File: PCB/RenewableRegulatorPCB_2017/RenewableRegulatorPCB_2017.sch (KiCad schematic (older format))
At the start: 39 parts, among them IC1 ATTINY84-P, K1 IO_0-2, K2 PWR, P1 INPUT, P2 ISP, P3 FTDI_OUTPUT, P4 DUMP1, P5 DUMP2, Q1 MOSFET_N, Q2 MOSFET_N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

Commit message: Updated PCB
First version of schematic. Needs review
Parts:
- removed C1: 10uf, symbol CP1-RESCUE-RenewableRegulatorPCB_2017
- removed C2: 100u, symbol CP1-RESCUE-RenewableRegulatorPCB_2017
- removed C4, C5: 100n, symbol C-RESCUE-RenewableRegulatorPCB_2017
- removed D1: 1N4001, symbol DIODE
- removed D3: RGB_LED, ~, symbol RGB_LED
- removed D4, D6: LED, symbol LED-RESCUE-RenewableRegulatorPCB_2017
- removed D5, D7: UF4001, symbol DIODE
- removed IC1: ATTINY84-P, DIP14, symbol ATTINY84-P-RESCUE-RenewableRegulatorPCB_2017
- removed K1: IO_0-2, symbol CONN_3
- removed K2: PWR, symbol CONN_3
- removed MH4: CONN_1, symbol CONN_1
- removed P2: ISP, symbol CONN_3X2
- removed P3: FTDI_OUTPUT, symbol CONN_6
- removed P4: DUMP1, symbol CONN_2
- removed Q1, Q2: MOSFET_N, symbol MOSFET_N
- removed R5: R, symbol R-RESCUE-RenewableRegulatorPCB_2017
- removed R6, R8: 1k, symbol R-RESCUE-RenewableRegulatorPCB_2017
- removed R7, R9: 100k, symbol R-RESCUE-RenewableRegulatorPCB_2017
- removed RV1, RV2: POT, symbol POT-RESCUE-RenewableRegulatorPCB_2017
- removed U1: 7805/LM2931, symbol 7805
- removed U2: TC427, ~, symbol TC427
- added C2: 100nf, matts_components:C1_wide_lg_pad, symbol C-RESCUE-RenewableRegulatorPCB_2017
- added C3: 100uf, REInnovationFootprint:C_1V7_TH, symbol CP
- added D2: 3v3, REInnovationFootprint:TH_Diode_1, symbol ZENER-RESCUE-RenewableRegulatorPCB_2017
- added D3, D4: 1N5819, REInnovationFootprint:TH_Diode_1, symbol D
- added D5: WS2811_5mm, REInnovationFootprint:TH_WS2811_LED_8mm, symbol WS2811_5mm
- added DISP1: OLED_I2C, matts_components:SIL-4_large_pad, symbol OLED_I2C
- added DISP2: SPI_LCD, matts_components:SIL-8_lg_pad_1mm, symbol CONN_01X08
- added ENC1: Encoder, REInnovationFootprint:TH_Encoder, symbol Encoder_1
- added F1: 1A, REInnovationFootprint:TH_MC36188_FUSE, symbol FUSE
- added J1: Arduino_Nano_Header, REInnovationFootprint:NANO_DIP_30_600, symbol Arduino_Nano_Header
- added J?: JACK_TRS_6PINS, symbol JACK_TRS_6PINS
- added P2: Vref?, matts_components:SIL-2_solder_connect, symbol CONN_01X02
- added P3: MicroSD, matts_components:SIL-6_large_pads_marker, symbol CONN_01X06
- added P4: SERIAL, matts_components:SIL-4_Grove_SIL, symbol CONN_01X04
- added VR1, VR2: VR, REInnovationFootprint:TH_MC36188_FUSE, symbol VR
- C1: renamed from C3; value 100n -> 100nf; footprint (none) -> matts_components:C1_wide_lg_pad
- D1: renamed from D2; value 5v1 -> 3v3; footprint (none) -> REInnovationFootprint:TH_Diode_1
- LOGO1: renamed from MH2; footprint (none) -> CuriousElectric3:CEC_Globe_10mm_FCU
- LOGO2: renamed from MH3; footprint (none) -> CuriousElectric3:CuriousElectric_flat_12mm
- P1: footprint (none) -> matts_components:SIL-2_screw_terminal_32A
- P5: value DUMP2 -> OUTPUT; footprint (none) -> matts_components:SIL-2_screw_terminal_32A
- R1, R2, R3, R4: footprint (none) -> REInnovationFootprint:TH_Resistor_1
- renumbered MH1 to PCB1
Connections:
- net labels added: +3V3, EN_A, EN_B, EN_SW, LCD_BL, LCD_CS, LCD_DC, LED_D, SCL, SDA, SD_CS, TEMP, VINm, VOUTm, Vinput, Voutput
- net labels removed: FET2, FEt1, RESET, V
- wire segments 157 -> 129
- no-connect marks 5 -> 4
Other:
- note added: "DS1820 1 Wire"
- note added: "Designed for max 30A current\nMust have 30A fuse in Battery Line"
- note added: "FET & CONTROL"
- note added: "MICRO CONTROLLER"
- note added: "OLED DISPLAY"
- note added: "PCB"
- note added: "POWER SUPPLY"
- note added: "RGB LED"
- note added: "ROTARY ENCODER"
- note added: "Reverse Polarity Protection\nWill blow control fuse if reversed."
- note added: "SD CARD MODULE"
- note added: "SERIAL OUTPUT"
- note added: "SPI 128x128 LCD"
- note added: "Temperature Sensor"
- note removed: "5V Power Supply"
- note removed: "FTDI CONNECTION"
- note removed: "MicroController ATTiny"
- note removed: "Mounting holes"
- note removed: "Programming port"
- note removed: "Serial Connection"
- moved on the sheet: C1, D1, LOGO1, LOGO2, P1, PCB1, R1, R2

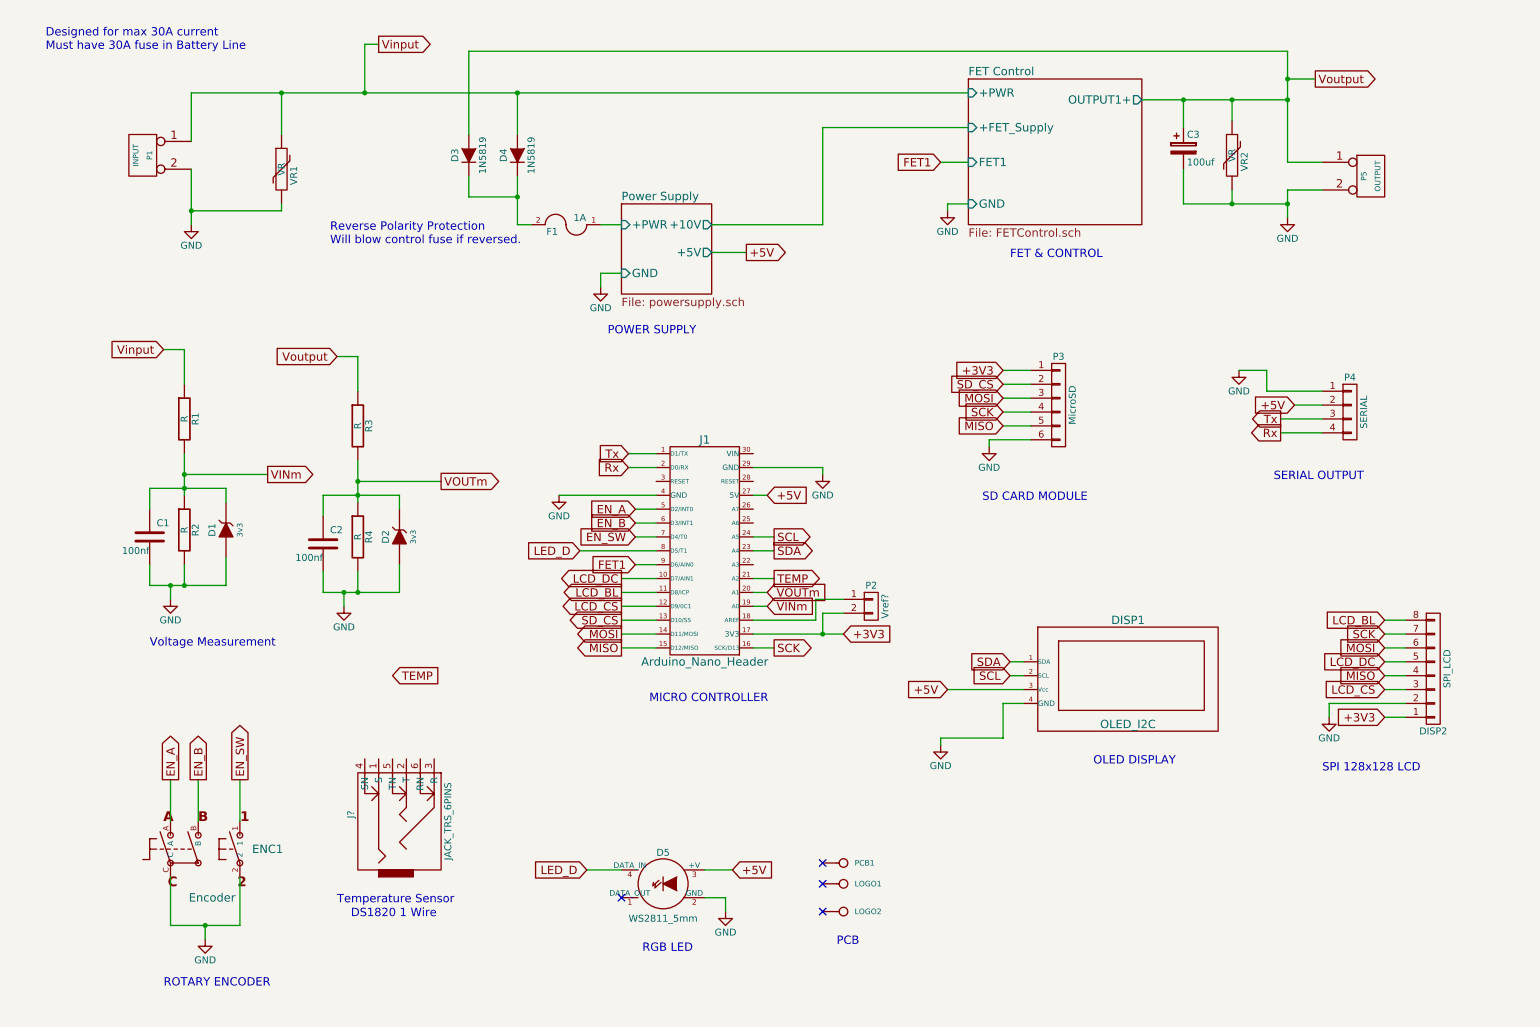
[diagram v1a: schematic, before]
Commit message: Moved code into new file structure
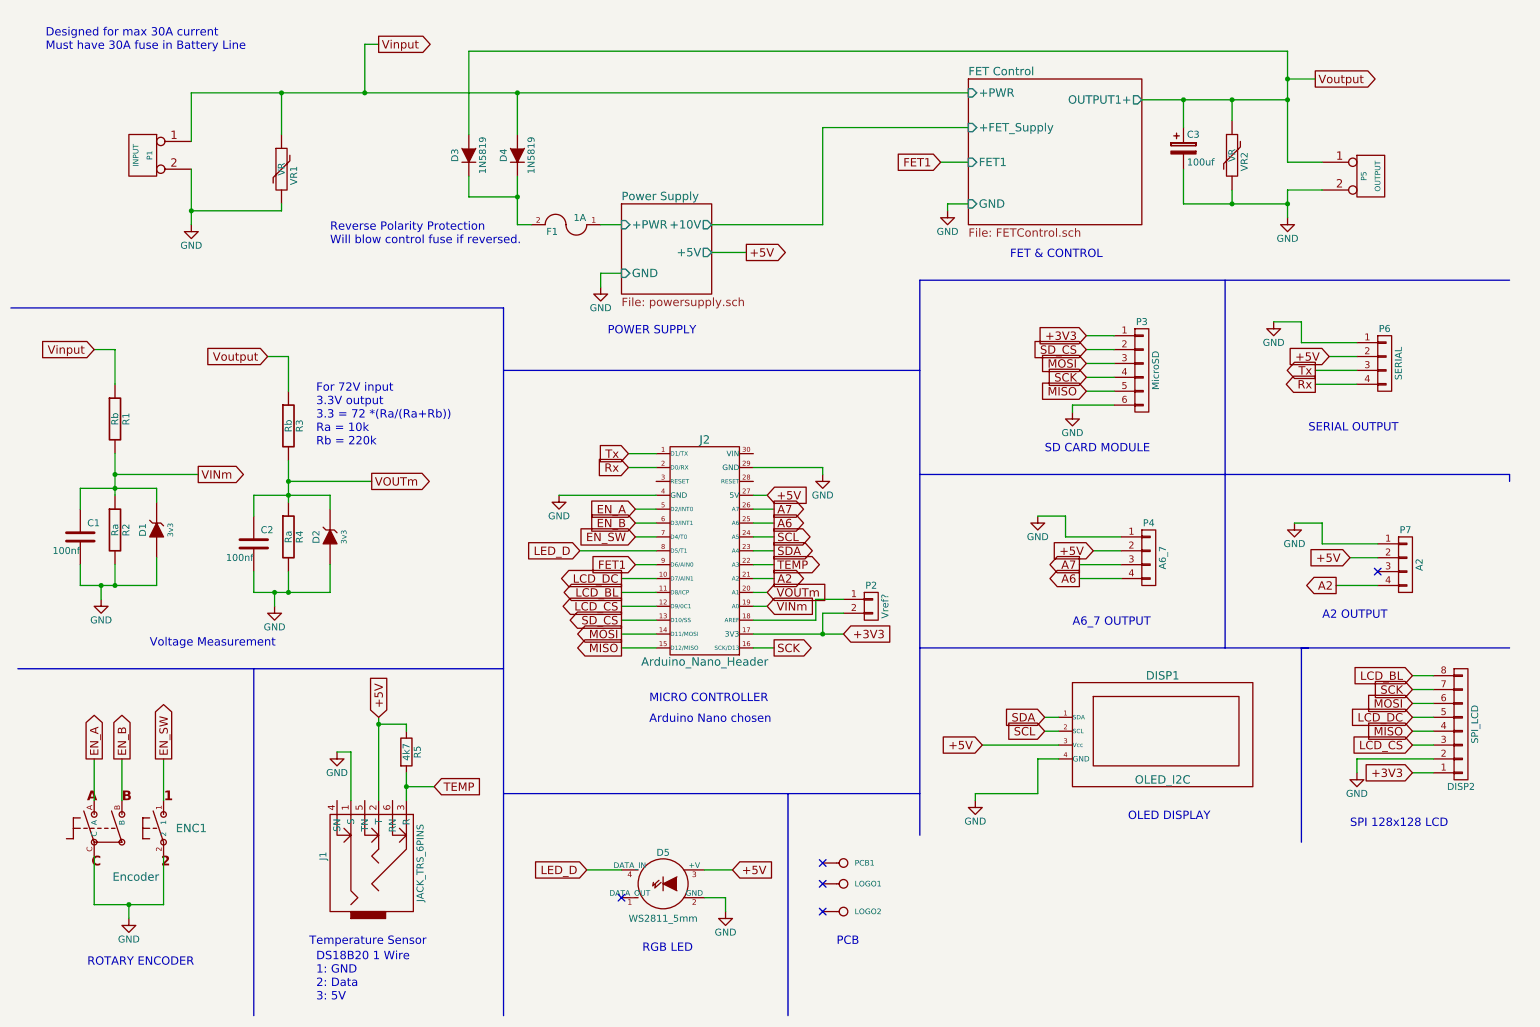
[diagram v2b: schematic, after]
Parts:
- added P4: A6_7, matts_components:SIL-4_Grove_SIL, symbol CONN_01X04
- added P7: A2, matts_components:SIL-4_Grove_SIL, symbol CONN_01X04
- added R5: 4k7, symbol R
- R1, R3: value R -> Rb
- R2, R4: value R -> Ra
- gave numbers to parts that had none: 1
- renumbered J1 to J2, P4 to P6
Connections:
- net +5V: now also J1.2 (T), P4.2 (P2), P7.2 (P2), R5.1
- net GND: now also J1.1 (S), P4.1 (P1), P7.1 (P1)
- net TEMP: now also J1.3 (R), J2.22 (A3), R5.2; no longer J2.21 (A2)
- net A6: now reaches J2.25 (A6)
- net A6: now also P4.4 (P4)
- net A7: now reaches J2.26 (A7)
- net A7: now also P4.3 (P3)
- new net A2: J2.21 (A2), P7.4 (P4)
- no-connect marks 4 -> 5
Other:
- note added: "A2 OUTPUT"
- note added: "A6_7 OUTPUT"
- note added: "Arduino Nano chosen"
- note added: "DS18B20 1 Wire\n1: GND\n2: Data\n3: 5V"
- note added: "For 72V input\n3.3V output\n3.3 = 72 *(Ra/(Ra+Rb))\nRa = 10k\nRb = 220k"
- note removed: "DS1820 1 Wire"
- moved on the sheet: C1, C2, D1, D2, DISP1, DISP2, ENC1, J1, P3, P6, R1, R2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

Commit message: Large update of PCB design
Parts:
- added EN1: PCB, ~, symbol CONN_1
- added P8: TP_Vin, matts_components:1pin_0_8mm, symbol CONN_01X01
- added P9: TP_Vout, matts_components:1pin_0_8mm, symbol CONN_01X01
- C3: Description (none) -> 100V Electrolytic; Manufacturer (none) -> Panasonic; Manufacturer Part No (none) -> ECA-2AM101B; Supplier 1 (none) -> RS; Supplier 1 Cost (none) -> 0.141; Supplier 1 Part No (none) -> 807-3431
- D5: Description (none) -> TH WS2811 Single LED Addressable; Supplier 1 (none) -> AliExpress
- DISP1: footprint matts_components:SIL-4_large_pad -> REInnovationFootprint:TH_OLED1306
- DISP2: footprint matts_components:SIL-8_lg_pad_1mm -> REInnovationFootprint:TH_LCD_SPI_128x128
- F1: value 1A -> 500mA; Manufacturer (none) -> TE; Manufacturer Part No (none) -> RXEF050; Supplier 1 (none) -> RS; Supplier 1 Cost (none) -> 0.263; Supplier 1 Part No (none) -> 517-6635
- J1: footprint (none) -> REInnovationFootprint:TH_3_5mm_Jack
- LOGO1: value CONN_1 -> LOGO
- LOGO2: value CONN_1 -> LOGO; footprint CuriousElectric3:CuriousElectric_flat_12mm -> CuriousElectric3:TCEC_Words_13mm
- P3: Description (none) -> External Micro SD slot with level shifter
- PCB1: value CONN_1 -> PCB; footprint (none) -> REInnovationFootprint:PCB_75x100mm
- R5: footprint (none) -> REInnovationFootprint:TH_Resistor_1
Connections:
- net VINm: now also P8.1 (P1)
- net VOUTm: now also P9.1 (P1)
- no-connect marks 5 -> 6
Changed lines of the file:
@@
 P 6450 7050
 F 0 "LOGO2" H 6530 7050 40  0000 L CNN
-F 1 "CONN_1" H 6450 7105 30  0001 C CNN
-F 2 "CuriousElectric3:CuriousElectric_flat_12mm" H 6450 7050 60  0001 C CNN
+F 1 "LOGO" H 6450 7105 30  0001 C CNN
+F 2 "CuriousElectric3:TCEC_Words_13mm" H 6450 7050 60  0001 C CNN
 F 3 "" H 6450 7050 60  0001 C CNN
+F 4 "~" H 6450 7050 60  0000 C CNN "Notes"
+F 5 "~" H 6450 7050 60  0001 C CNN "Description"
+F 6 "~" H 6450 7050 60  0001 C CNN "Manufacturer"
+F 7 "~" H 6450 7050 60  0001 C CNN "Manufacturer Part No"
+F 8 "~" H 6450 7050 60  0001 C CNN "Supplier 1"
+F 9 "~" H 6450 7050 60  0001 C CNN "Supplier 1 Part No"
+F 10 "~" H 6450 7050 60  0001 C CNN "Supplier 1 Cost"
+F 11 "~" H 6450 7050 60  0001 C CNN "Supplier 2"
+F 12 "~" H 6450 7050 60  0001 C CNN "Supplier 2 Part No"
+F 13 "~" H 6450 7050 60  0001 C CNN "Supplier 2 Cost"
 	1    6450 7050
 	1    0    0    -1
@@
 P 6450 6850
 F 0 "LOGO1" H 6530 6850 40  0000 L CNN
-F 1 "CONN_1" H 6450 6905 30  0001 C CNN
+F 1 "LOGO" H 6450 6905 30  0001 C CNN
 F 2 "CuriousElectric3:CEC_Globe_10mm_FCU" H 6450 6850 60  0001 C CNN
 F 3 "" H 6450 6850 60  0001 C CNN
+F 4 "~" H 6450 6850 60  0000 C CNN "Notes"
+F 5 "~" H 6450 6850 60  0001 C CNN "Description"
+F 6 "~" H 6450 6850 60  0001 C CNN "Manufacturer"
+F 7 "~" H 6450 6850 60  0001 C CNN "Manufacturer Part No"
+F 8 "~" H 6450 6850 60  0001 C CNN "Supplier 1"
+F 9 "~" H 6450 6850 60  0001 C CNN "Supplier 1 Part No"
+F 10 "~" H 6450 6850 60  0001 C CNN "Supplier 1 Cost"
+F 11 "~" H 6450 6850 60  0001 C CNN "Supplier 2"
+F 12 "~" H 6450 6850 60  0001 C CNN "Supplier 2 Part No"
+F 13 "~" H 6450 6850 60  0001 C CNN "Supplier 2 Cost"
 	1    6450 6850
 	1    0    0    -1
@@
 P 6450 6700
 F 0 "PCB1" H 6530 6700 40  0000 L CNN
-F 1 "CONN_1" H 6450 6755 30  0001 C CNN
-F 2 "" H 6450 6700 60  0001 C CNN
+F 1 "PCB" H 6450 6755 30  0001 C CNN
+F 2 "REInnovationFootprint:PCB_75x100mm" H 6450 6700 60  0001 C CNN
 F 3 "" H 6450 6700 60  0001 C CNN
+F 4 "~" H 6450 6700 60  0000 C CNN "Notes"
+F 5 "~" H 6450 6700 60  0001 C CNN "Description"
+F 6 "~" H 6450 6700 60  0001 C CNN "Manufacturer"
+F 7 "~" H 6450 6700 60  0001 C CNN "Manufacturer Part No"
+F 8 "~" H 6450 6700 60  0001 C CNN "Supplier 1"
+F 9 "~" H 6450 6700 60  0001 C CNN "Supplier 1 Part No"
+F 10 "~" H 6450 6700 60  0001 C CNN "Supplier 1 Cost"
+F 11 "~" H 6450 6700 60  0001 C CNN "Supplier 2"
+F 12 "~" H 6450 6700 60  0001 C CNN "Supplier 2 Part No"
+F 13 "~" H 6450 6700 60  0001 C CNN "Supplier 2 Cost"
 	1    6450 6700
 	1    0    0    -1
@@
 P 950 4350
 F 0 "C1" H 1000 4450 50  0000 L CNN
-F 1 "100nf" H 750 4250 50  0000 L CNN
+F 1 "100nf" H 700 4200 50  0000 L CNN
 F 2 "matts_components:C1_wide_lg_pad" H 950 4350 60  0001 C CNN
 F 3 "" H 950 4350 60  0001 C CNN
@@
 P 4450 2100
 F 0 "F1" H 4550 2150 50  0000 C CNN
-F 1 "1A" H 4350 2050 50  0000 C CNN
+F 1 "500mA" H 4350 2050 50  0000 C CNN
 F 2 "REInnovationFootprint:TH_MC36188_FUSE" H 4450 2100 50  0001 C CNN
 F 3 "" H 4450 2100 50  0000 C CNN
 F 4 "~" H 4450 2100 60  0000 C CNN "Notes"
 F 5 "Resettable Fuse 60V" H 4450 2100 60  0001 C CNN "Description"
-F 6 "~" H 4450 2100 60  0001 C CNN "Manufacturer"
-F 7 "~" H 4450 2100 60  0001 C CNN "Manufacturer Part No"
-F 8 "~" H 4450 2100 60  0001 C CNN "Supplier 1"
-F 9 "~" H 4450 2100 60  0001 C CNN "Supplier 1 Part No"
-F 10 "~" H 4450 2100 60  0001 C CNN "Supplier 1 Cost"
+F 6 "TE" H 4450 2100 60  0001 C CNN "Manufacturer"
+F 7 "RXEF050" H 4450 2100 60  0001 C CNN "Manufacturer Part No"
+F 8 "RS" H 4450 2100 60  0001 C CNN "Supplier 1"
+F 9 "517-6635" H 4450 2100 60  0001 C CNN "Supplier 1 Part No"
+F 10 "0.263" H 4450 2100 60  0001 C CNN "Supplier 1 Cost"
 F 11 "~" H 4450 2100 60  0001 C CNN "Supplier 2"
 F 12 "~" H 4450 2100 60  0001 C CNN "Supplier 2 Part No"
@@
 F 0 "DISP1" H 8750 7350 60  0000 C CNN
 F 1 "OLED_I2C" H 8750 6600 60  0000 C CNN
-F 2 "matts_components:SIL-4_large_pad" H 9750 6700 60  0001 C CNN
+F 2 "REInnovationFootprint:TH_OLED1306" H 9750 6700 60  0001 C CNN
 F 3 "" H 9750 6700 60  0000 C CNN
 F 4 "~" H 8350 6350 60  0000 C CNN "Notes"
@@
 F 1 "WS2811_5mm" H 5150 6600 50  0000 C CNN
 F 2 "REInnovationFootprint:TH_WS2811_LED_8mm" H 5150 6850 50  0001 C CNN
-F 3 "" H 5150 6850 50  0000 C CNN
+F 3 "https://www.coolcomponents.co.uk/en/opto/leds/digital-rgb-addressable-led-5mm-through-hole-10-pack.html" H 5150 6850 50  0001 C CNN
 F 4 "~" H 5150 6850 60  0000 C CNN "Notes"
-F 5 "~" H 5150 6850 60  0001 C CNN "Description"
+F 5 "TH WS2811 Single LED Addressable" H 5150 6850 60  0001 C CNN "Description"
 F 6 "~" H 5150 6850 60  0001 C CNN "Manufacturer"
 F 7 "~" H 5150 6850 60  0001 C CNN "Manufacturer Part No"
-F 8 "~" H 5150 6850 60  0001 C CNN "Supplier 1"
+F 8 "AliExpress" H 5150 6850 60  0001 C CNN "Supplier 1"
 F 9 "~" H 5150 6850 60  0001 C CNN "Supplier 1 Part No"
 F 10 "~" H 5150 6850 60  0001 C CNN "Supplier 1 Cost"
@@
 F 1 "MicroSD" V 8700 3150 50  0000 C CNN
 F 2 "matts_components:SIL-6_large_pads_marker" H 8600 3150 50  0001 C CNN
-F 3 "" H 8600 3150 50  0000 C CNN
+F 3 "http://www.gearbest.com/development-boards/pp_63013.html?currency=GBP&vip=760169&gclid=CPHFuoqAjdMCFUK7GwodO08Omw" H 8600 3150 50  0001 C CNN
+F 4 "~" H 8600 3150 60  0000 C CNN "Notes"
+F 5 "External Micro SD slot with level shifter" H 8600 3150 60  0001 C CNN "Description"
+F 6 "~" H 8600 3150 60  0001 C CNN "Manufacturer"
+F 7 "~" H 8600 3150 60  0001 C CNN "Manufacturer Part No"
+F 8 "~" H 8600 3150 60  0001 C CNN "Supplier 1"
+F 9 "~" H 8600 3150 60  0001 C CNN "Supplier 1 Part No"
+F 10 "~" H 8600 3150 60  0001 C CNN "Supplier 1 Cost"
+F 11 "~" H 8600 3150 60  0001 C CNN "Supplier 2"
+F 12 "~" H 8600 3150 60  0001 C CNN "Supplier 2 Part No"
+F 13 "~" H 8600 3150 60  0001 C CNN "Supplier 2 Cost"
 	1    8600 3150
 	1    0    0    -1
@@
 P 2200 4400
 F 0 "C2" H 2250 4500 50  0000 L CNN
-F 1 "100nf" H 2000 4300 50  0000 L CNN
+F 1 "100nf" H 1950 4250 50  0000 L CNN
 F 2 "matts_components:C1_wide_lg_pad" H 2200 4400 60  0001 C CNN
 F 3 "" H 2200 4400 60  0001 C CNN
@@
 F 0 "DISP2" H 10900 6150 50  0000 C CNN
 F 1 "SPI_LCD" V 11000 5700 50  0000 C CNN
-F 2 "matts_components:SIL-8_lg_pad_1mm" H 10900 5700 50  0001 C CNN
+F 2 "REInnovationFootprint:TH_LCD_SPI_128x128" H 10900 5700 50  0001 C CNN
 F 3 "https://www.elecrow.com/wiki/index.php?title=1.44%27%27_128x_128_TFT_LCD_with_SPI_Interface" H 10900 5700 50  0001 C CNN
 F 4 "~" H 10900 5700 60  0000 C CNN "Notes"
@@
 F 2 "REInnovationFootprint:C_1V7_TH" H 8938 1400 50  0001 C CNN
 F 3 "" H 8900 1550 50  0000 C CNN
+F 4 "~" H 8900 1550 60  0000 C CNN "Notes"
+F 5 "100V Electrolytic" H 8900 1550 60  0001 C CNN "Description"
+F 6 "Panasonic" H 8900 1550 60  0001 C CNN "Manufacturer"
+F 7 "ECA-2AM101B" H 8900 1550 60  0001 C CNN "Manufacturer Part No"
+F 8 "RS" H 8900 1550 60  0001 C CNN "Supplier 1"
+F 9 "807-3431" H 8900 1550 60  0001 C CNN "Supplier 1 Part No"
+F 10 "0.141" H 8900 1550 60  0001 C CNN "Supplier 1 Cost"
+F 11 "~" H 8900 1550 60  0001 C CNN "Supplier 2"
+F 12 "~" H 8900 1550 60  0001 C CNN "Supplier 2 Part No"
+F 13 "~" H 8900 1550 60  0001 C CNN "Supplier 2 Cost"
 	1    8900 1550
 	1    0    0    -1
@@
 F 0 "J1" H 3100 7050 50  0000 C CNN
 F 1 "JACK_TRS_6PINS" H 3050 6350 50  0000 C CNN
-F 2 "" H 3200 6500 50  0000 C CNN
+F 2 "REInnovationFootprint:TH_3_5mm_Jack" H 3200 6500 50  0001 C CNN
 F 3 "" H 3200 6500 50  0000 C CNN
 	1    3100 6650
@@
 F 0 "R5" V 3380 5900 50  0000 C CNN
 F 1 "4k7" V 3300 5900 50  0000 C CNN
-F 2 "" V 3230 5900 50  0000 C CNN
+F 2 "REInnovationFootprint:TH_Resistor_1" V 3230 5900 50  0001 C CNN
 F 3 "" H 3300 5900 50  0000 C CNN
 	1    3300 5900
@@
 Text Notes 5050 5700 0    60   ~ 0
 Arduino Nano chosen
+$Comp
+L CONN_01X01 P9
+U 1 1 58E529B4
+P 3150 4550
+F 0 "P9" H 3150 4650 50  0000 C CNN
+F 1 "TP_Vout" V 3250 4550 50  0000 C CNN
+F 2 "matts_components:1pin_0_8mm" H 3150 4550 50  0001 C CNN
+F 3 "" H 3150 4550 50  0000 C CNN
+F 4 "~" H 3150 4550 60  0000 C CNN "Notes"
+F 5 "~" H 3150 4550 60  0001 C CNN "Description"
+F 6 "~" H 3150 4550 60  0001 C CNN "Manufacturer"
+F 7 "~" H 3150 4550 60  0001 C CNN "Manufacturer Part No"
+F 8 "~" H 3150 4550 60  0001 C CNN "Supplier 1"
+F 9 "~" H 3150 4550 60  0001 C CNN "Supplier 1 Part No"
+F 10 "~" H 3150 4550 60  0001 C CNN "Supplier 1 Cost"
+F 11 "~" H 3150 4550 60  0001 C CNN "Supplier 2"
+F 12 "~" H 3150 4550 60  0001 C CNN "Supplier 2 Part No"
+F 13 "~" H 3150 4550 60  0001 C CNN "Supplier 2 Cost"
+	1    3150 4550
+	1    0    0    -1
+$EndComp
+$Comp
+L CONN_01X01 P8
+U 1 1 58E52AD3
+P 1750 3600
+F 0 "P8" H 1750 3700 50  0000 C CNN
+F 1 "TP_Vin" V 1850 3600 50  0000 C CNN
+F 2 "matts_components:1pin_0_8mm" H 1750 3600 50  0001 C CNN
+F 3 "" H 1750 3600 50  0000 C CNN
+	1    1750 3600
+	1    0    0    -1
+$EndComp
+Wire Wire Line
+	2950 4550 2950 3950
+Connection ~ 2950 3950
+Wire Wire Line
+	1550 3600 1550 3900
+Connection ~ 1550 3900
+NoConn ~ 6300 6500
+$Comp
+L CONN_1 EN1
+U 1 1 58E55463
+P 6450 6500
+F 0 "EN1" H 6530 6500 40  0000 L CNN
+F 1 "PCB" H 6450 6555 30  0001 C CNN
+F 2 "~" H 6450 6500 60  0001 C CNN
+F 3 "http://cpc.farnell.com/hammond/1590bb/box-diecast-119x94x30/dp/EN82042?ost=EN82042&selectedCategoryId=&categoryNameResp=All&searchView=table&iscrfnonsku=false" H 6450 6500 60  0001 C CNN
+F 4 "~" H 6450 6500 60  0000 C CNN "Notes"
+F 5 "Enclosure for unit" H 6450 6500 60  0001 C CNN "Description"
+F 6 "~" H 6450 6500 60  0001 C CNN "Manufacturer"
+F 7 "~" H 6450 6500 60  0001 C CNN "Manufacturer Part No"
+F 8 "~" H 6450 6500 60  0001 C CNN "Supplier 1"
+F 9 "~" H 6450 6500 60  0001 C CNN "Supplier 1 Part No"
+F 10 "~" H 6450 6500 60  0001 C CNN "Supplier 1 Cost"
+F 11 "~" H 6450 6500 60  0001 C CNN "Supplier 2"
+F 12 "~" H 6450 6500 60  0001 C CNN "Supplier 2 Part No"
+F 13 "~" H 6450 6500 60  0001 C CNN "Supplier 2 Cost"
+	1    6450 6500
+	1    0    0    -1
+$EndComp
 $EndSCHEMATC
